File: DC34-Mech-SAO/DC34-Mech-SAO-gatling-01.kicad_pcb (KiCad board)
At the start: 2 copper layers, 34.2 x 44.4 mm, 23 parts, among them J1 Conn_01x06_Male, J2 Conn_01x01_Male, U1 ATtiny816-M

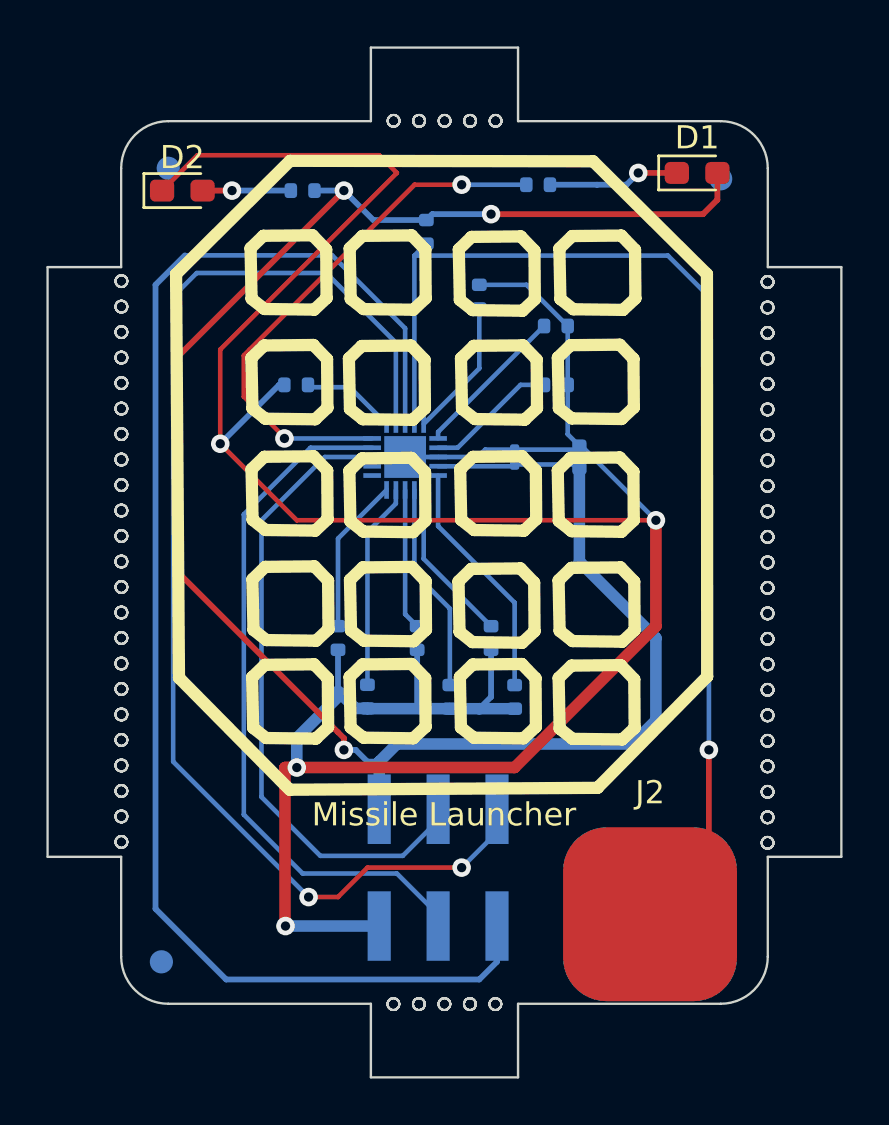
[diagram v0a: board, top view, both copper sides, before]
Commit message: Panelized Design
Put all 5 designs on a panel.
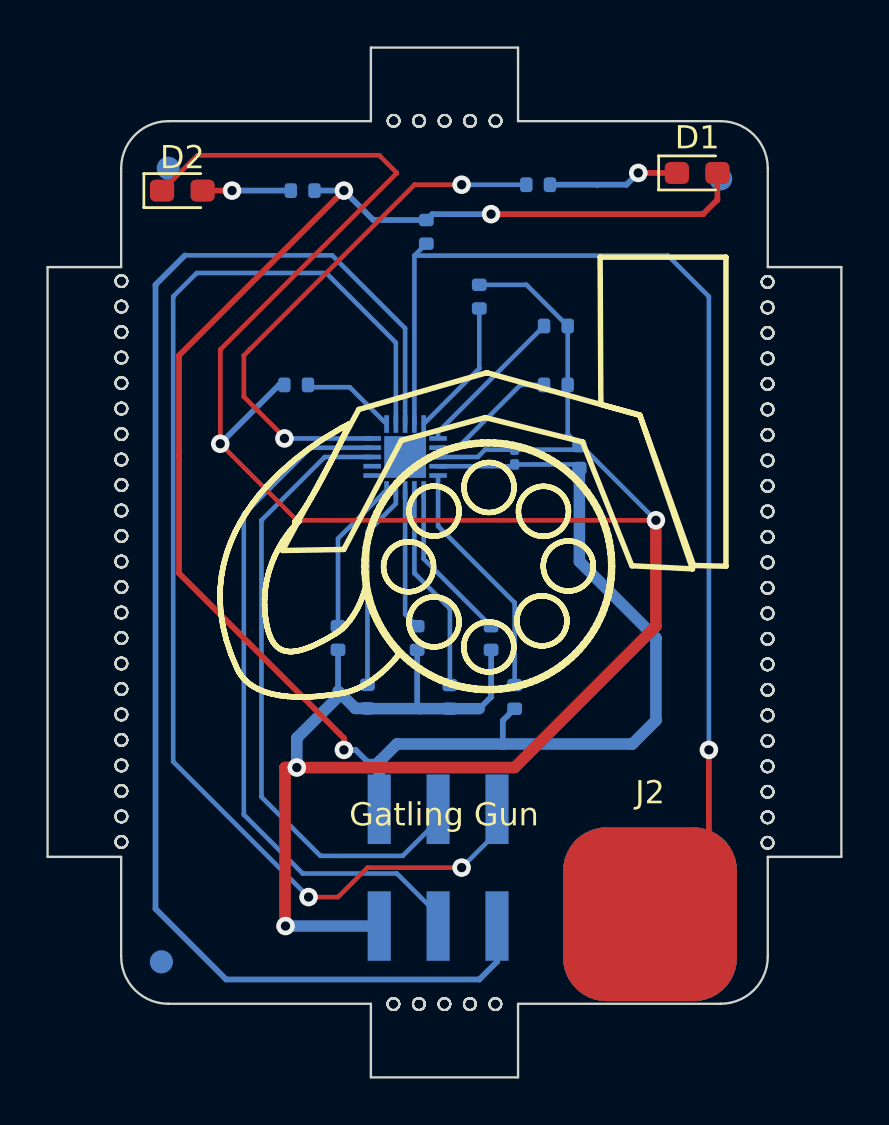
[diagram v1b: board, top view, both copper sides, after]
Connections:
- R4 pad 2: GND -> PWR
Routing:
- net PWR: track 84.4 -> 86.1 mm
- net GND: track 125.7 -> 124.2 mm
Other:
- board text added: "Gatling Gun"
- board text removed: "Missile Launcher"
